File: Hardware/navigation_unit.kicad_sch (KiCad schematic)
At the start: 37 parts, among them U4 STM32F405RGT6, U5 TDD01H0SB1R, U6 TDD01H0SB1R, Y1 25MHz

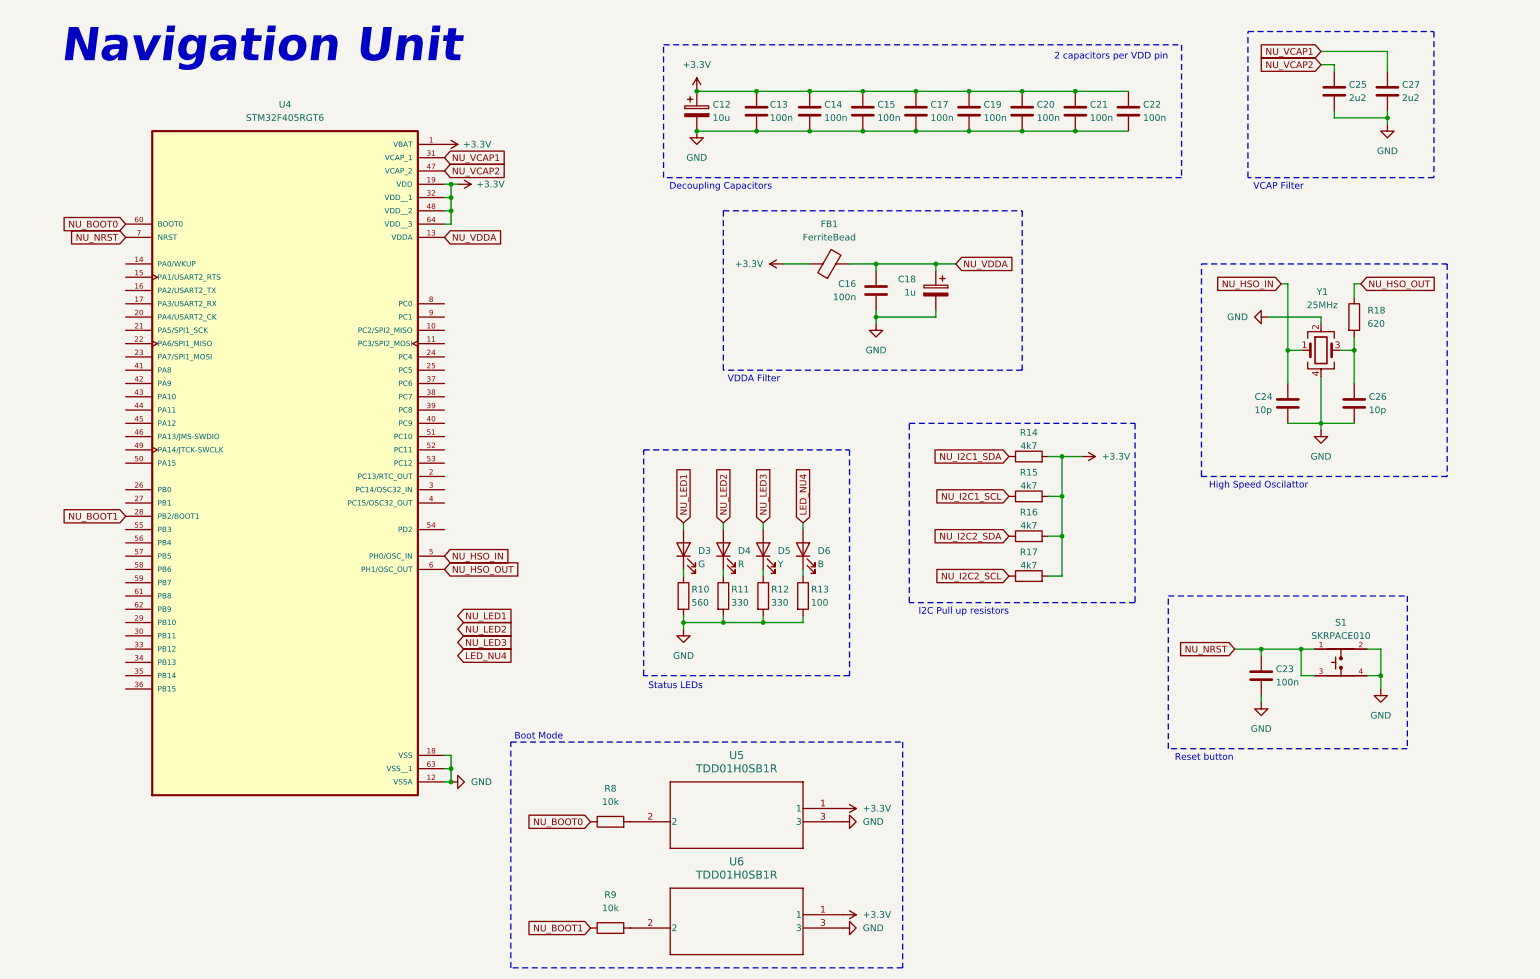
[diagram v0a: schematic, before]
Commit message: fcu, nu schematics, problem with pins
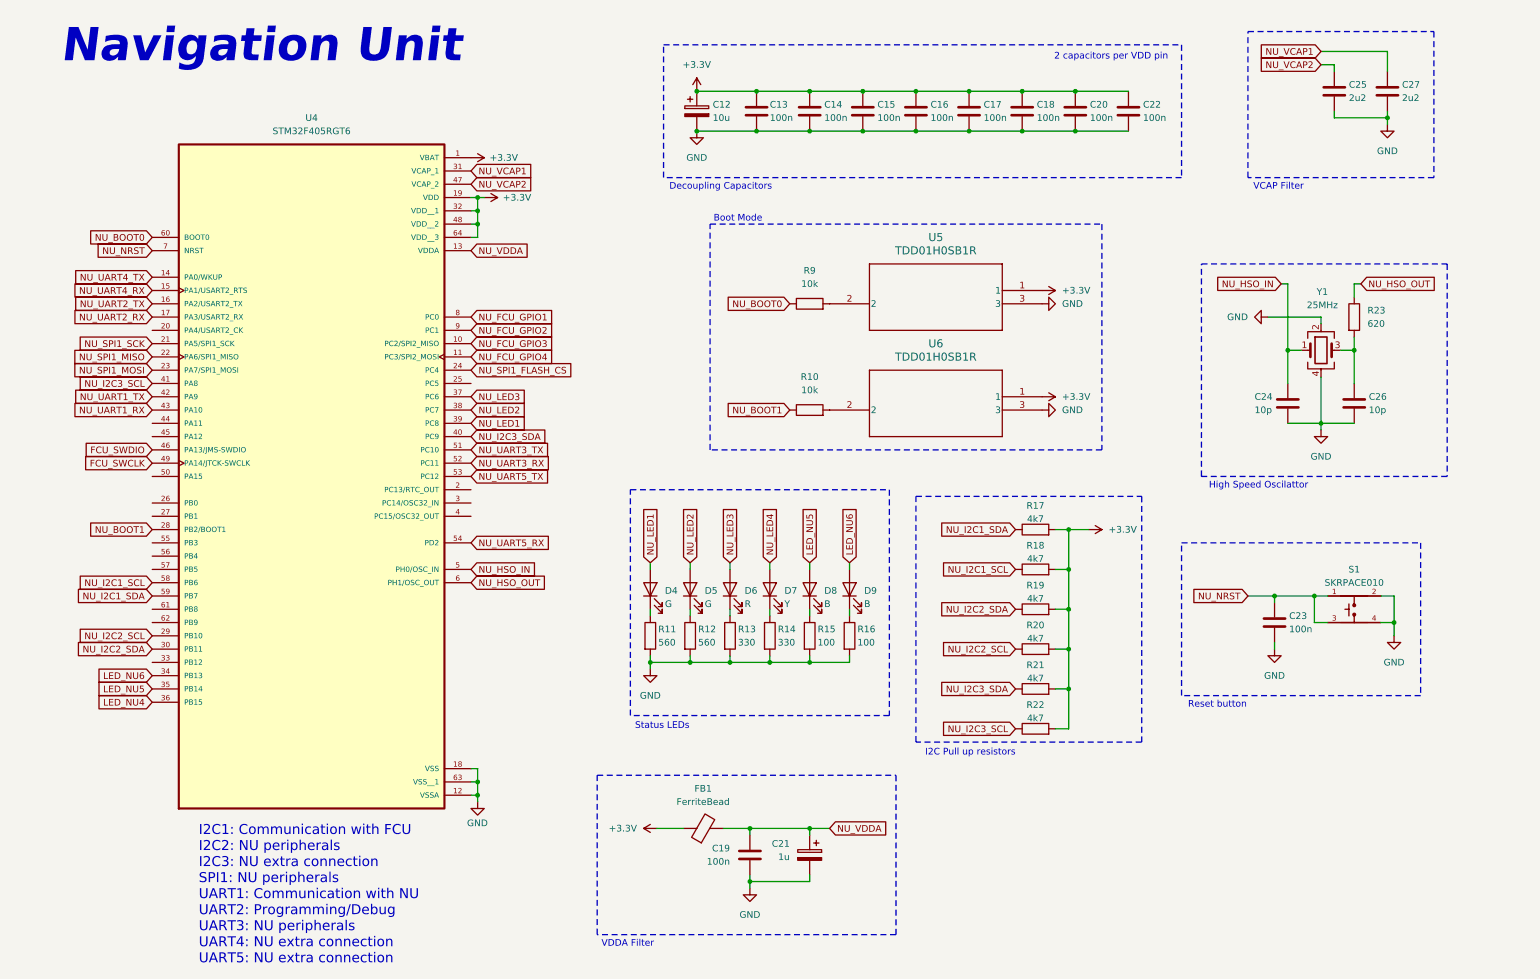
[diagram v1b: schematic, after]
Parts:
- added D4: G, symbol Device:LED
- added D9: B, symbol Device:LED
- added R11: 560, symbol Device:R
- added R16: 100, symbol Device:R
- added R21, R22: 4k7, symbol Device:R
- renumbered C17 to C16, C19 to C17, C20 to C18, C16 to C19, C21 to C20, C18 to C21, D3 to D5, D4 to D6, D5 to D7, D6 to D8, R9 to R10, R10 to R12, R11 to R13, R12 to R14, R13 to R15, R14 to R17, R15 to R18, R16 to R19, R17 to R20, R18 to R23, R8 to R9
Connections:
- net +3.3V: now also R21.2, R22.2
- net GND: now also R11.2, R16.2
- net LED_NU4: now also U4.36 (PB15); no longer D8.2 (A)
- net NU_I2C1_SCL: now also U4.58 (PB6)
- net NU_I2C1_SDA: now also U4.59 (PB7)
- net NU_I2C2_SCL: now also U4.29 (PB10)
- net NU_I2C2_SDA: now also U4.30 (PB11)
- net NU_LED1: now also U4.39 (PC8), D4.2 (A); no longer D5.2 (A)
- net NU_LED2: now also D5.2 (A), U4.38 (PC7); no longer D6.2 (A)
- net NU_LED3: now also D6.2 (A), U4.37 (PC6); no longer D7.2 (A)
- net NU_FCU_GPIO3: now reaches U4.10 (PC2/SPI2_MISO)
- net NU_FCU_GPIO4: now reaches U4.11 (PC3/SPI2_MOSI)
- net NU_UART4_TX: now reaches U4.14 (PA0/WKUP)
- net NU_UART4_RX: now reaches U4.15 (PA1/USART2_RTS)
- net NU_UART2_TX: now reaches U4.16 (PA2/USART2_TX)
- net NU_UART2_RX: now reaches U4.17 (PA3/USART2_RX)
- net NU_SPI1_SCK: now reaches U4.21 (PA5/SPI1_SCK)
- net NU_SPI1_MISO: now reaches U4.22 (PA6/SPI1_MISO)
- net NU_SPI1_MOSI: now reaches U4.23 (PA7/SPI1_MOSI)
- net NU_SPI1_FLASH_CS: now reaches U4.24 (PC4)
- net LED_NU6: now reaches U4.34 (PB13)
- net LED_NU6: now also D9.2 (A)
- net LED_NU5: now reaches U4.35 (PB14)
- net LED_NU5: now also D8.2 (A)
- net NU_I2C3_SDA: now reaches U4.40 (PC9)
- net NU_I2C3_SDA: now also R21.1
- net NU_I2C3_SCL: now reaches U4.41 (PA8)
- net NU_I2C3_SCL: now also R22.1
- net NU_UART1_TX: now reaches U4.42 (PA9)
- net NU_UART1_RX: now reaches U4.43 (PA10)
- net FCU_SWDIO: now reaches U4.46 (PA13/JMS-SWDIO)
- net FCU_SWCLK: now reaches U4.49 (PA14/JTCK-SWCLK)
- net NU_UART3_TX: now reaches U4.51 (PC10)
- net NU_UART3_RX: now reaches U4.52 (PC11)
- net NU_UART5_TX: now reaches U4.53 (PC12)
- net NU_UART5_RX: now reaches U4.54 (PD2)
- net NU_FCU_GPIO1: now reaches U4.8 (PC0)
- net NU_FCU_GPIO2: now reaches U4.9 (PC1)
- new net: D4.1 (K), R11.1
- new net: D9.1 (K), R16.1
- new net NU_LED4: D7.2 (A)
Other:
- note added: "I2C1: Communication with FCU I2C2: NU peripherals I2C3: NU extra connection SPI1: NU peripherals UART1: Communication with NU UART2: Programming/Debug UART3: NU peripherals UART4: NU extra connection UART5: NU extra connection"
- moved on the sheet: C19, C21, C23, D5, D6, D7, D8, FB1, R10, R12, R13, R14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

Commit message: pin mess up win, starting over again
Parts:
- removed C12: 10u, symbol Device:C_Polarized
- removed C13, C14, C15, C16, C17, C18, C19, C20, C22, C23: 100n, symbol Device:C
- removed C21: 1u, symbol Device:C_Polarized
- removed C24, C26: 10p, symbol Device:C
- removed C25, C27: 2u2, symbol Device:C
- removed D4, D5: G, symbol Device:LED
- removed D6: R, symbol Device:LED
- removed D7: Y, symbol Device:LED
- removed D8, D9: B, symbol Device:LED
- removed FB1: FerriteBead, symbol Device:FerriteBead
- removed R10, R9: 10k, symbol Device:R
- removed R11, R12: 560, symbol Device:R
- removed R13, R14: 330, symbol Device:R
- removed R15, R16: 100, symbol Device:R
- removed R17, R18, R19, R20, R21, R22: 4k7, symbol Device:R
- removed R23: 620, symbol Device:R
- removed S1: SKRPACE010, SKRPACE010:SW_SKRPACE010, symbol Aircraft_Components:SKRPACE010
- removed U4: STM32F405RGT6, STM32F405RGT6:QFP50P1200X1200X160-64N, symbol Aircraft_Components:STM32F405RGT6
- removed U5, U6: TDD01H0SB1R, SOT_TDDSB1R_CNK, symbol Aircraft_Components:TDD01H0SB1R
- removed Y1: 25MHz, symbol Device:Crystal_GND24
- added U4: STM32F405RGTx, Package_QFP:LQFP-64_10x10mm_P0.5mm, symbol MCU_ST_STM32F4:STM32F405RGTx
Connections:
- new net: U4.18 (VSS), U4.63 (VSS)
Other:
- note removed: "2 capacitors per VDD pin"
- note removed: "Boot Mode"
- note removed: "Decoupling Capacitors"
- note removed: "High Speed Oscilattor"
- note removed: "I2C Pull up resistors"
- note removed: "I2C1: Communication with FCU I2C2: NU peripherals I2C3: NU extra connection SPI1: NU peripherals UART1: Communication with NU UART2: Programming/Debug UART3: NU peripherals UART4: NU extra connection UART5: NU extra connection"
- note removed: "Navigation Unit"
- note removed: "Reset button"
- note removed: "Status LEDs"
- note removed: "VCAP Filter"
- note removed: "VDDA Filter"

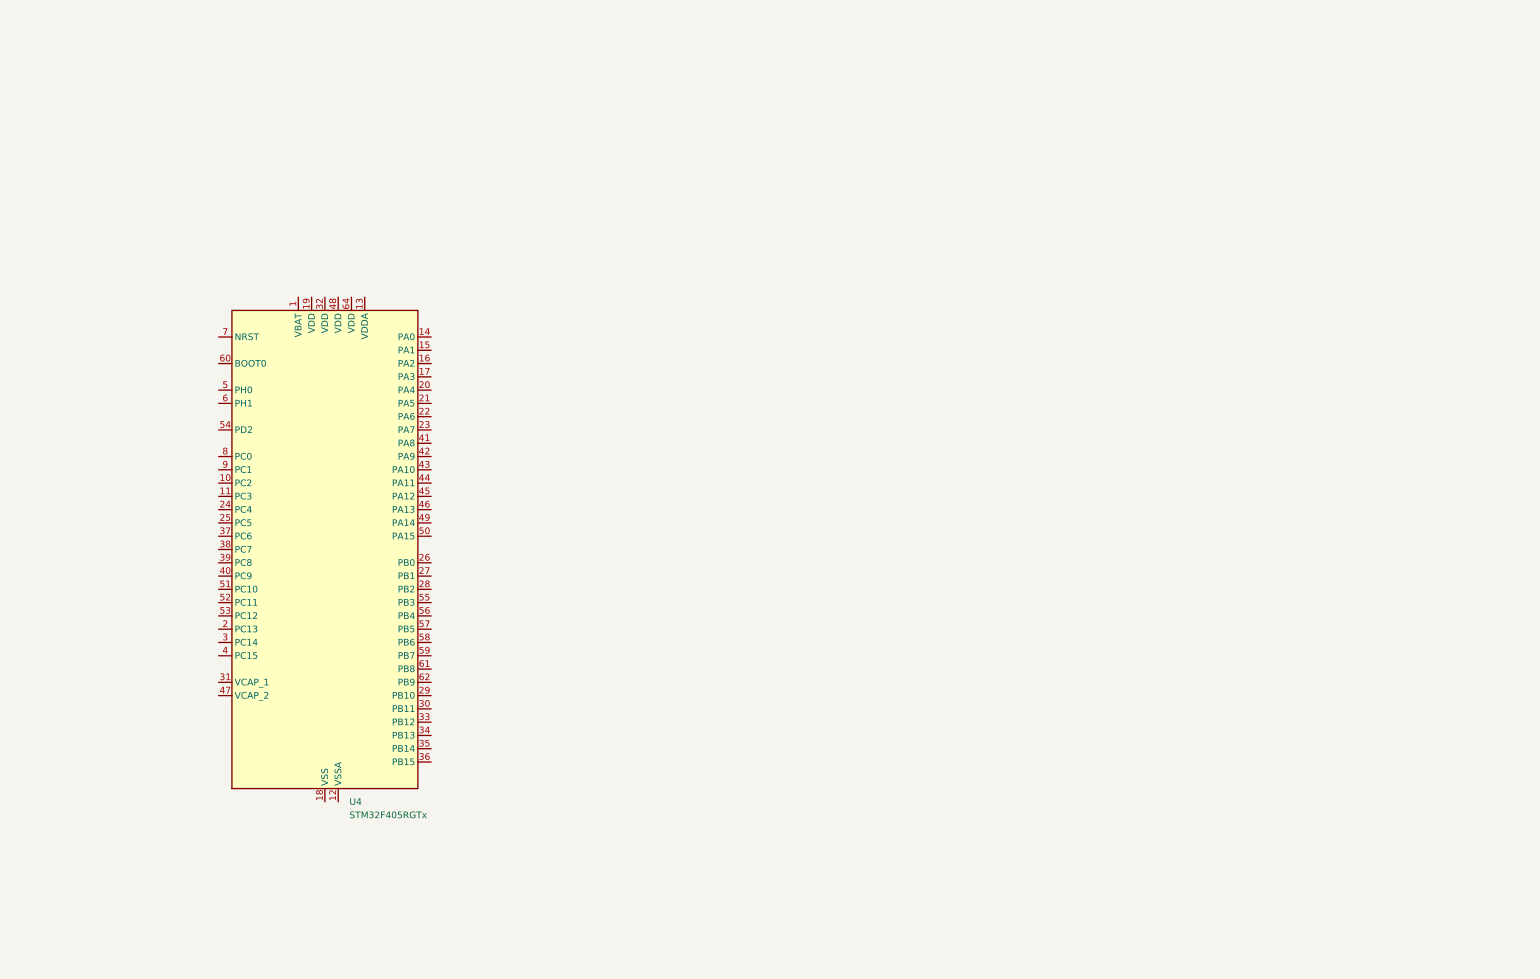
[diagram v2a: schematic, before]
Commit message: added projects, schematic almost done, need revision
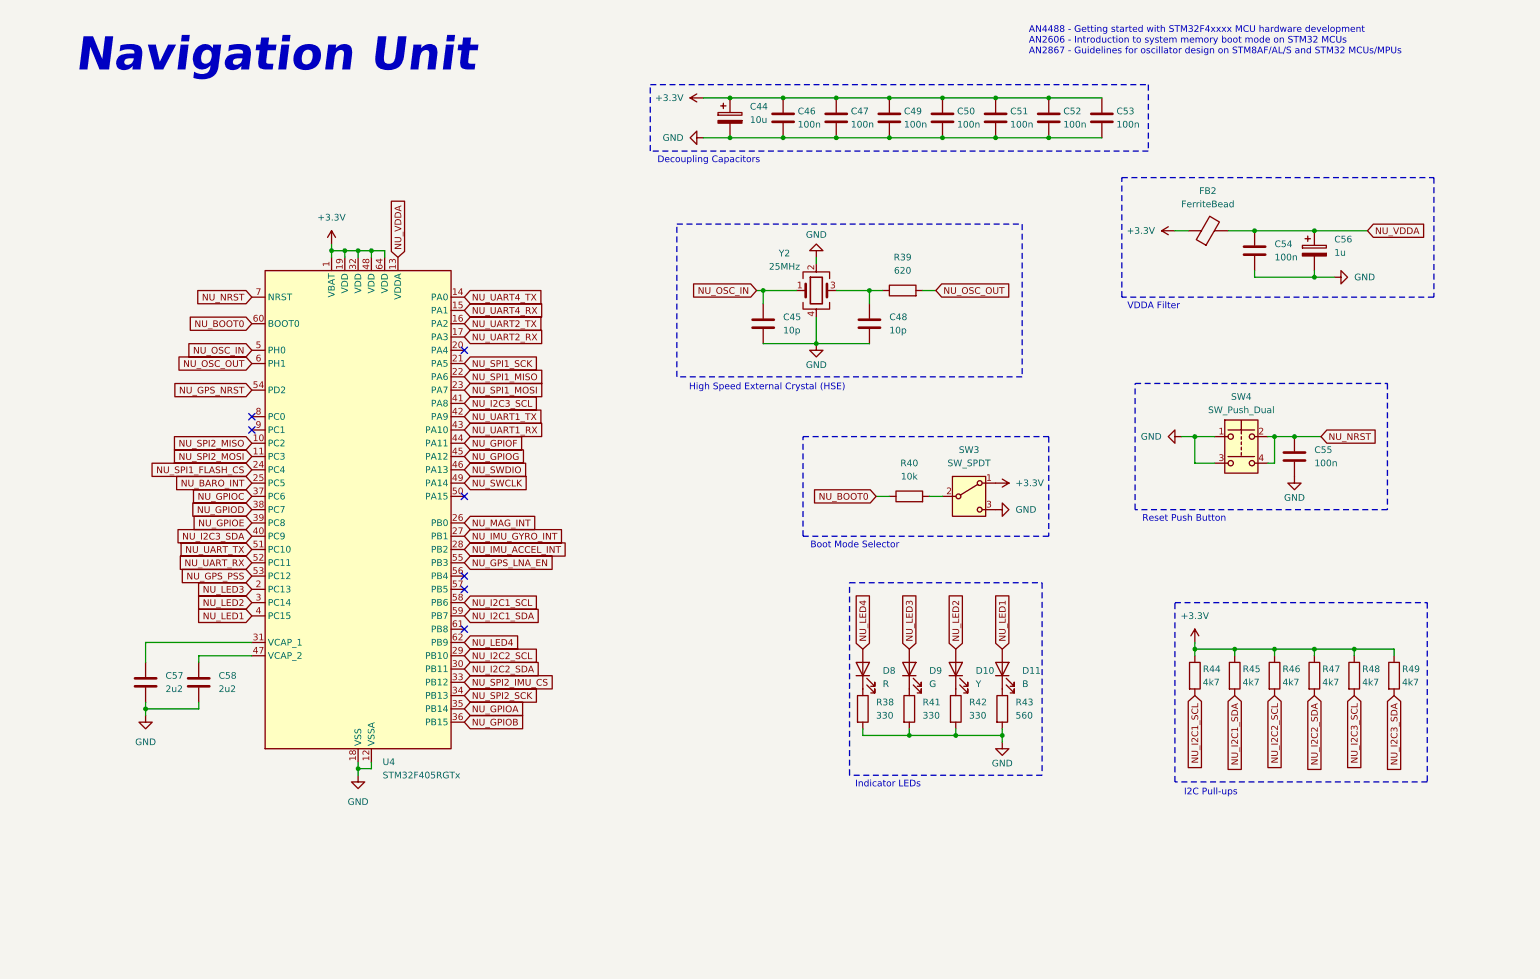
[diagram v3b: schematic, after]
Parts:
- added C44: 10u, symbol Device:C_Polarized
- added C45, C48: 10p, symbol Device:C
- added C46, C47, C49, C50, C51, C52, C53, C54, C55: 100n, symbol Device:C
- added C56: 1u, symbol Device:C_Polarized
- added C57, C58: 2u2, symbol Device:C
- added D10: Y, symbol Device:LED
- added D11: B, symbol Device:LED
- added D8: R, symbol Device:LED
- added D9: G, symbol Device:LED
- added FB2: FerriteBead, symbol Device:FerriteBead
- added R38, R41, R42: 330, symbol Device:R
- added R39: 620, symbol Device:R
- added R40: 10k, symbol Device:R
- added R43: 560, symbol Device:R
- added R44, R45, R46, R47, R48, R49: 4k7, symbol Device:R
- added SW3: SW_SPDT, symbol Switch:SW_SPDT
- added SW4: SW_Push_Dual, symbol Switch:SW_Push_Dual
- added Y2: 25MHz, symbol Device:Crystal_GND24
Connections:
- net +3.3V: now reaches U4.1 (VBAT)
- net +3.3V: now also U4.19 (VDD), U4.32 (VDD), U4.48 (VDD), U4.64 (VDD), C44.1, C46.1, C47.1, C49.1, C50.1, C51.1, C52.1, C53.1, FB2.1, R44.1, R45.1, R46.1, R47.1, R48.1, R49.1, SW3.1 (A)
- net NU_SPI2_MISO: now reaches U4.10 (PC2)
- net NU_SPI2_MOSI: now reaches U4.11 (PC3)
- net GND: now reaches U4.12 (VSSA)
- net GND: now also U4.18 (VSS), U4.63 (VSS), C44.2, C45.2, C46.2, C47.2, C48.2, C49.2, C50.2, C51.2, C52.2, C53.2, C54.2, C55.2, C56.2, C57.2, C58.2, R38.2, R41.2, R42.2, R43.2, SW3.3 (C), SW4.1, SW4.3, Y2.2, Y2.4
- net NU_VDDA: now reaches U4.13 (VDDA)
- net NU_VDDA: now also C54.1, C56.1, FB2.2
- net NU_UART4_TX: now reaches U4.14 (PA0)
- net NU_UART4_RX: now reaches U4.15 (PA1)
- net NU_UART2_TX: now reaches U4.16 (PA2)
- net NU_UART2_RX: now reaches U4.17 (PA3)
- net NU_LED3: now reaches U4.2 (PC13)
- net NU_LED3: now also D9.2 (A)
- net NU_SPI1_SCK: now reaches U4.21 (PA5)
- net NU_SPI1_MISO: now reaches U4.22 (PA6)
- net NU_SPI1_MOSI: now reaches U4.23 (PA7)
- net NU_SPI1_FLASH_CS: now reaches U4.24 (PC4)
- net NU_BARO_INT: now reaches U4.25 (PC5)
- net NU_MAG_INT: now reaches U4.26 (PB0)
- net NU_IMU_GYRO_INT: now reaches U4.27 (PB1)
- net NU_IMU_ACCEL_INT: now reaches U4.28 (PB2)
- net NU_I2C2_SCL: now reaches U4.29 (PB10)
- net NU_I2C2_SCL: now also R46.2
- net NU_LED2: now reaches U4.3 (PC14)
- net NU_LED2: now also D10.2 (A)
- net NU_I2C2_SDA: now reaches U4.30 (PB11)
- net NU_I2C2_SDA: now also R47.2
- net at U4.31 (VCAP_1): now also C57.1
- net NU_SPI2_IMU_CS: now reaches U4.33 (PB12)
- net NU_SPI2_SCK: now reaches U4.34 (PB13)
- net NU_GPIOA: now reaches U4.35 (PB14)
- net NU_GPIOB: now reaches U4.36 (PB15)
- net NU_GPIOC: now reaches U4.37 (PC6)
- net NU_GPIOD: now reaches U4.38 (PC7)
- net NU_GPIOE: now reaches U4.39 (PC8)
- net NU_LED1: now reaches U4.4 (PC15)
- net NU_LED1: now also D11.2 (A)
- net NU_I2C3_SDA: now reaches U4.40 (PC9)
- net NU_I2C3_SDA: now also R49.2
- net NU_I2C3_SCL: now reaches U4.41 (PA8)
- net NU_I2C3_SCL: now also R48.2
- net NU_UART1_TX: now reaches U4.42 (PA9)
- net NU_UART1_RX: now reaches U4.43 (PA10)
- net NU_GPIOF: now reaches U4.44 (PA11)
- net NU_GPIOG: now reaches U4.45 (PA12)
- net NU_SWDIO: now reaches U4.46 (PA13)
- net at U4.47 (VCAP_2): now also C58.1
- net NU_SWCLK: now reaches U4.49 (PA14)
- net NU_OSC_IN: now reaches U4.5 (PH0)
- net NU_OSC_IN: now also C45.1, Y2.1
- net NU_UART_TX: now reaches U4.51 (PC10)
- net NU_UART_RX: now reaches U4.52 (PC11)
- net NU_GPS_PSS: now reaches U4.53 (PC12)
- net NU_GPS_NRST: now reaches U4.54 (PD2)
- net NU_GPS_LNA_EN: now reaches U4.55 (PB3)
- net NU_I2C1_SCL: now reaches U4.58 (PB6)
- net NU_I2C1_SCL: now also R44.2
- net NU_I2C1_SDA: now reaches U4.59 (PB7)
- net NU_I2C1_SDA: now also R45.2
- net NU_OSC_OUT: now reaches U4.6 (PH1)
- net NU_OSC_OUT: now also R39.2
- net NU_BOOT0: now reaches U4.60 (BOOT0)
- net NU_BOOT0: now also R40.1
- net NU_LED4: now reaches U4.62 (PB9)
- net NU_LED4: now also D8.2 (A)
- net NU_NRST: now reaches U4.7 (NRST)
- net NU_NRST: now also C55.1, SW4.2, SW4.4
- new net: R40.2, SW3.2 (B)
- new net: D8.1 (K), R38.1
- new net: D10.1 (K), R42.1
- new net: C48.1, R39.1, Y2.3
- new net: D9.1 (K), R41.1
- new net: D11.1 (K), R43.1
- no-connect marks 0 -> 7
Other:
- note added: "AN4488 - Getting started with STM32F4xxxx MCU hardware development AN2606 - Introduction to system memory boot mode on STM32 MCUs AN2867 - Guidelines for oscillator design on STM8AF/AL/S and STM32 MCUs/MPUs"
- note added: "Boot Mode Selector"
- note added: "Decoupling Capacitors"
- note added: "High Speed External Crystal (HSE)"
- note added: "I2C Pull-ups"
- note added: "Indicator LEDs"
- note added: "Navigation Unit"
- note added: "Reset Push Button"
- note added: "VDDA Filter"
- moved on the sheet: U4

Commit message: version 0.1.0
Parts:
- renumbered C57 to C12, C58 to C13, C44 to C14, C45 to C15, C46 to C16, C47 to C17, C48 to C18, C49 to C19, C50 to C20, C51 to C21, C52 to C22, C53 to C23, C54 to C24, C55 to C25, C56 to C26, D8 to D4, D9 to D5, D10 to D6, D11 to D7, FB2 to FB1, R39 to R10, R40 to R11, R41 to R12, R42 to R13, R43 to R14, R44 to R15, R45 to R16, R46 to R17, R47 to R18, R48 to R19, R49 to R20, R38 to R9, SW3 to SW1, SW4 to SW2, Y2 to Y1
